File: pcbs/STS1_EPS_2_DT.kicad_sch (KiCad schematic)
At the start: 19 parts, among them Q2 SI7272DP-T1-GE3, Q3 2N7002, U1 4072, U2 LTC6995IDCB-1

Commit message: Fixed some warnings and errors.
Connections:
- net +5V is gone; now on net V_LOGIC: R7.1
- net GND: no longer U1.1
- no-connect marks 0 -> 1
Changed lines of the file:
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@@
 		(color 0 0 0 0)
 	)
+	(no_connect
+		(at 107.95 113.03)
+	)
 	(wire
 		(pts
@@
 	(wire
 		(pts
+			(xy 107.95 113.03) (xy 105.41 113.03)
+		)
+		(stroke
+			(width 0)
+			(type default)
+		)
+	)
+	(wire
+		(pts
 			(xy 128.27 135.89) (xy 128.27 137.16)
 		)
@@
 		)
 	)
-	(hierarchical_label "V_LOGIC"
-		(shape input)
-		(at 120.65 120.65 180)
+	(hierarchical_label "DT_SIGNAL"
+		(shape output)
+		(at 273.05 73.66 0)
 		(fields_autoplaced yes)
 		(effects
@@
 				(size 1.27 1.27)
 			)
-			(justify right)
+			(justify left)
 		)
 	)
-	(hierarchical_label "DT_SIGNAL"
-		(shape output)
-		(at 273.05 73.66 0)
+	(hierarchical_label "V_LOGIC"
+		(shape input)
+		(at 97.79 20.32 0)
 		(fields_autoplaced yes)
 		(effects
@@
 	(hierarchical_label "V_LOGIC"
 		(shape input)
-		(at 97.79 20.32 0)
+		(at 128.27 121.92 180)
 		(fields_autoplaced yes)
 		(effects
@@
 				(size 1.27 1.27)
 			)
-			(justify left)
+			(justify right)
 		)
 	)
@@
 	(symbol
 		(lib_id "power:GND")
-		(at 105.41 113.03 90)
-		(unit 1)
-		(exclude_from_sim no)
-		(in_bom yes)
-		(on_board yes)
-		(dnp no)
-		(fields_autoplaced yes)
-		(property "Reference" "#PWR024"
-			(at 111.76 113.03 0)
-			(effects
-				(font
-					(size 1.27 1.27)
-				)
-				(hide yes)
-			)
-		)
-		(property "Value" "GND"
-			(at 109.22 113.0299 90)
-			(effects
-				(font
-					(size 1.27 1.27)
-				)
-				(justify right)
-			)
-		)
-		(property "Footprint" ""
-			(at 105.41 113.03 0)
-			(effects
-				(font
-					(size 1.27 1.27)
-				)
-				(hide yes)
-			)
-		)
-		(property "Datasheet" ""
-			(at 105.41 113.03 0)
-			(effects
-				(font
-					(size 1.27 1.27)
-				)
-				(hide yes)
-			)
-		)
-		(property "Description" ""
-			(at 105.41 113.03 0)
-			(effects
-				(font
-					(size 1.27 1.27)
-				)
-				(hide yes)
-			)
-		)
-		(pin "1"
-		)
-		(instances
-			(project "STS1_EPS_2"
-				(path "/38c03ff7-ea47-4d00-b37d-ddcaa7d87722/d08cc104-26df-403e-aeed-bb3c2e21e328"
-					(reference "#PWR024")
-					(unit 1)
-				)
-			)
-		)
-	)
-	(symbol
-		(lib_id "power:GND")
 		(at 90.17 111.76 270)
 		(unit 1)
@@
 			)
 		)
-		(property "Description" ""
+		(property "Description" "Power symbol creates a global label with name \"GND\" , ground"
 			(at 90.17 111.76 0)
 			(effects
@@
 			)
 		)
-		(property "Description" ""
+		(property "Description" "Power symbol creates a global label with name \"GND\" , ground"
 			(at 90.17 114.3 0)
 			(effects
@@
 			)
 		)
-		(property "Description" ""
+		(property "Description" "Power symbol creates a global label with name \"GND\" , ground"
 			(at 148.59 97.79 0)
 			(effects
@@
 			)
 		)
-		(property "Description" ""
+		(property "Description" "Power symbol creates a global label with name \"GND\" , ground"
 			(at 146.05 129.54 0)
 			(effects
@@
 			)
 		)
-		(property "Description" ""
+		(property "Description" "Power symbol creates a global label with name \"GND\" , ground"
 			(at 196.85 97.79 0)
 			(effects
@@
 			)
 		)
-		(property "Description" ""
+		(property "Description" "Power symbol creates a global label with name \"GND\" , ground"
 			(at 158.75 85.09 0)
 			(effects
@@
 			)
 		)
-		(property "Description" ""
+		(property "Description" "Power symbol creates a global label with name \"GND\" , ground"
 			(at 90.17 99.06 0)
 			(effects
@@
 			)
 		)
-		(property "Description" ""
+		(property "Description" "Power symbol creates a global label with name \"GND\" , ground"
 			(at 219.71 97.79 0)
 			(effects
@@
 			)
 		)
-		(property "Description" ""
+		(property "Description" "Power symbol creates a global label with name \"GND\" , ground"
 			(at 90.17 109.22 0)
 			(effects
@@
 			)
 		)
-		(property "Description" ""
+		(property "Description" "0.115A Id, 60V Vds, N-Channel MOSFET, SOT-23"
 			(at 234.95 87.63 0)
 			(effects
@@
 			)
 		)
-		(property "Description" ""
+		(property "Description" "Power symbol creates a global label with name \"GND\" , ground"
 			(at 128.27 147.32 0)
 			(effects
@@
 			)
 		)
-		(property "Description" ""
+		(property "Description" "Power symbol creates a global label with name \"GND\" , ground"
 			(at 90.17 116.84 0)
 			(effects
@@
 			)
 		)
-		(property "Description" ""
+		(property "Description" "Power symbol creates a global label with name \"GND\" , ground"
 			(at 175.26 97.79 0)
 			(effects
@@
 			)
 		)
-		(property "Description" ""
+		(property "Description" "Power symbol creates a global label with name \"GND\" , ground"
 			(at 97.79 53.34 0)
 			(effects
@@
 	)
 	(symbol
-		(lib_id "power:+5V")
-		(at 128.27 121.92 0)
-		(unit 1)
-		(exclude_from_sim no)
-		(in_bom yes)
-		(on_board yes)
-		(dnp no)
-		(fields_autoplaced yes)
-		(property "Reference" "#PWR0112"
-			(at 128.27 125.73 0)
-			(effects
-				(font
-					(size 1.27 1.27)
-				)
-				(hide yes)
-			)
-		)
-		(property "Value" "+5V"
-			(at 128.27 116.84 0)
-			(effects
-				(font
-					(size 1.27 1.27)
-				)
-			)
-		)
-		(property "Footprint" ""
-			(at 128.27 121.92 0)
-			(effects
-				(font
-					(size 1.27 1.27)
-				)
-				(hide yes)
-			)
-		)
-		(property "Datasheet" ""
-			(at 128.27 121.92 0)
-			(effects
-				(font
-					(size 1.27 1.27)
-				)
-				(hide yes)
-			)
-		)
-		(property "Description" ""
-			(at 128.27 121.92 0)
-			(effects
-				(font
-					(size 1.27 1.27)
-				)
-				(hide yes)
-			)
-		)
-		(pin "1"
-		)
-		(instances
-			(project "STS1_EPS_2"
-				(path "/38c03ff7-ea47-4d00-b37d-ddcaa7d87722/d08cc104-26df-403e-aeed-bb3c2e21e328"
-					(reference "#PWR0112")
-					(unit 1)
-				)
-			)
-		)
-	)
-	(symbol
 		(lib_id "power:GND")
 		(at 237.49 97.79 0)
@@
 			)
 		)
-		(property "Description" ""
+		(property "Description" "Power symbol creates a global label with name \"GND\" , ground"
 			(at 237.49 97.79 0)
 			(effects

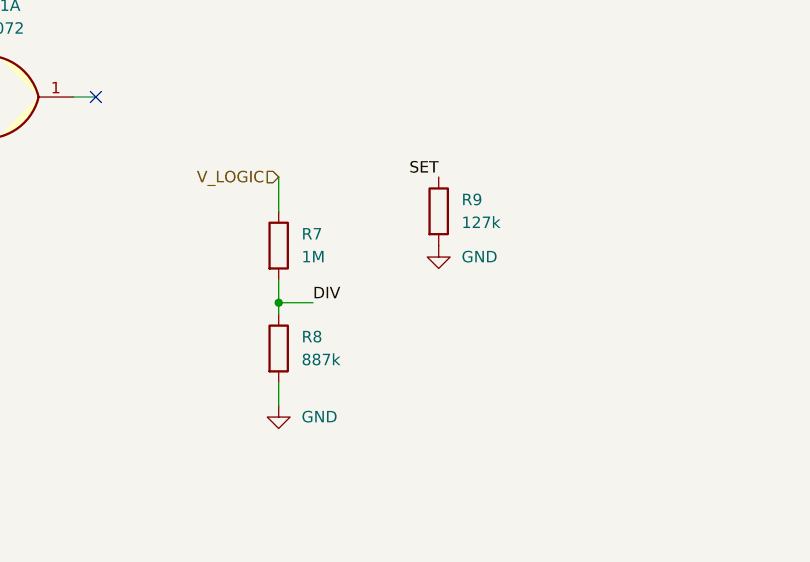
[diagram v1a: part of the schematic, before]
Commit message: Modified some resistor values slightly, so that they fall in common resistor series.
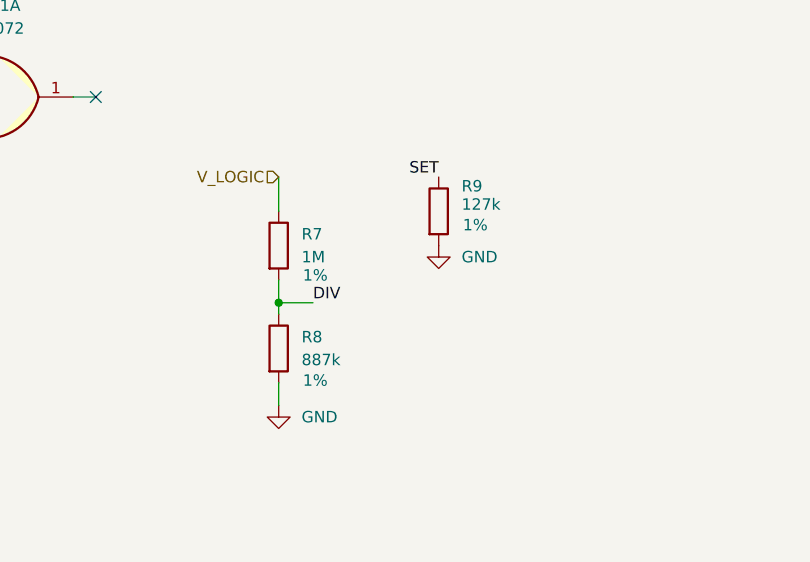
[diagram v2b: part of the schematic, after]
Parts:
- R7, R8, R9: Tolerance (none) -> 1%
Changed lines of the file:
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@@
 		(on_board yes)
 		(dnp no)
-		(fields_autoplaced yes)
 		(property "Reference" "R8"
 			(at 130.81 139.6999 0)
@@
 				)
 				(hide yes)
+			)
+		)
+		(property "Tolerance" "1%"
+			(at 132.334 144.526 0)
+			(effects
+				(font
+					(size 1.27 1.27)
+				)
 			)
 		)
@@
 		(on_board yes)
 		(dnp no)
-		(fields_autoplaced yes)
 		(property "Reference" "R7"
 			(at 130.81 128.2699 0)
@@
 				)
 				(hide yes)
+			)
+		)
+		(property "Tolerance" "1%"
+			(at 132.334 132.842 0)
+			(effects
+				(font
+					(size 1.27 1.27)
+				)
 			)
 		)
@@
 		(on_board yes)
 		(dnp no)
-		(fields_autoplaced yes)
 		(property "Reference" "R9"
-			(at 148.59 124.4599 0)
+			(at 148.59 122.9359 0)
 			(effects
 				(font
@@
 		)
 		(property "Value" "127k"
-			(at 148.59 126.9999 0)
+			(at 148.59 124.968 0)
 			(effects
 				(font
@@
 			)
 		)
+		(property "Tolerance" "1%"
+			(at 150.114 127.254 0)
+			(effects
+				(font
+					(size 1.27 1.27)
+				)
+			)
+		)

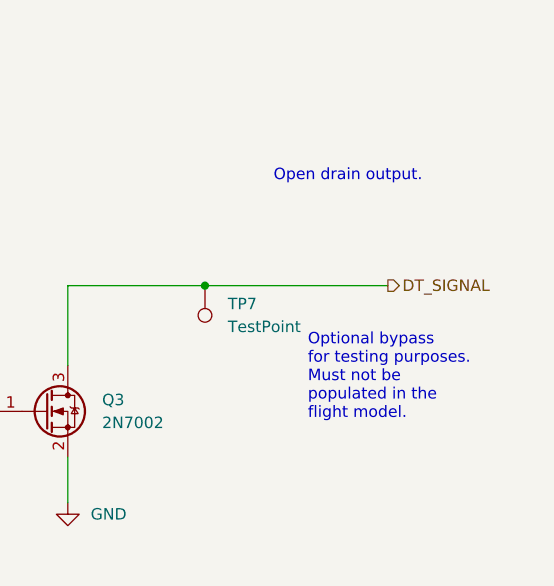
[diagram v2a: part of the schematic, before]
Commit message: Marked optional bypasses as "Do not place".
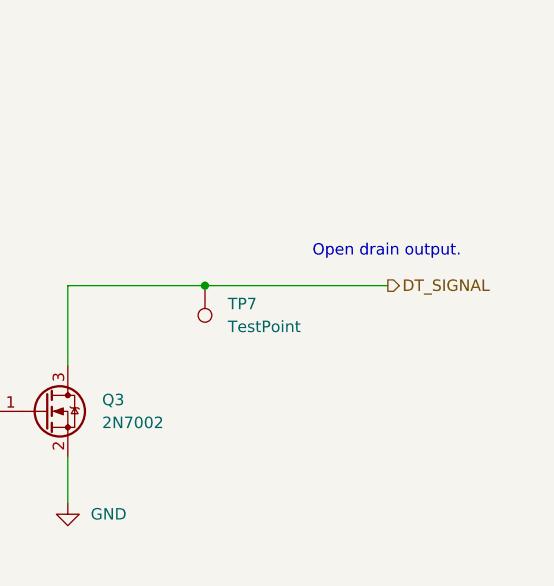
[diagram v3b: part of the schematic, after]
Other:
- note removed: "Optional bypass for testing purposes. Must not be populated in the flight model."
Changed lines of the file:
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@@
 	(text "Open drain output."
 		(exclude_from_sim no)
-		(at 260.35 62.23 0)
+		(at 264.668 70.612 0)
 		(effects
 			(font
@@
 		)
 	)
-	(text "Optional bypass \nfor testing purposes.\nMust not be \npopulated in the \nflight model."
-		(exclude_from_sim no)
-		(at 264.16 83.82 0)
-		(effects
-			(font
-				(size 1.27 1.27)
-			)
-			(justify left)
-		)
-	)

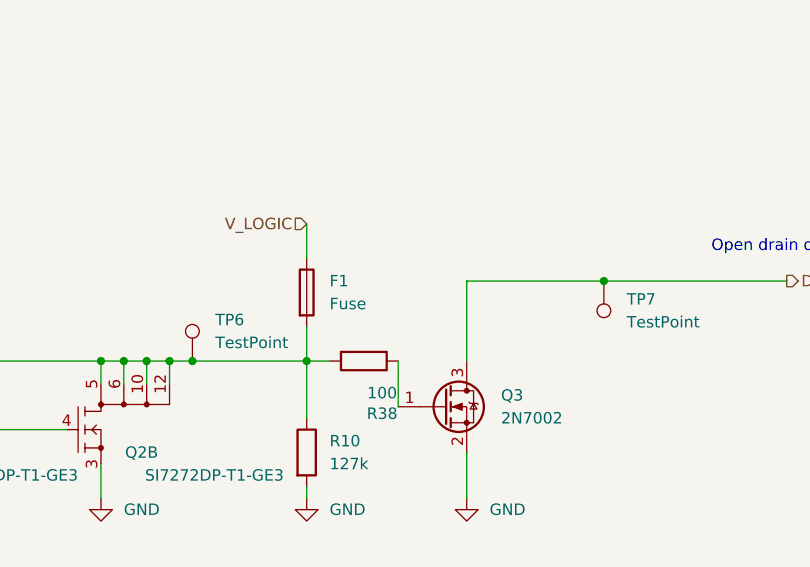
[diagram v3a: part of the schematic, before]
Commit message: Added part number to fuse.
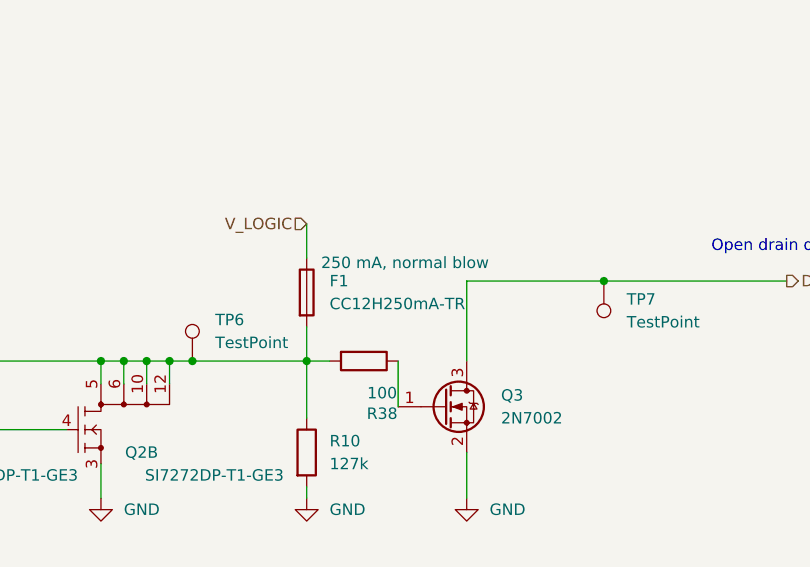
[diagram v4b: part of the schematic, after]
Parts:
- F1: value Fuse -> CC12H250mA-TR
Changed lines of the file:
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@@
 		(on_board yes)
 		(dnp no)
-		(fields_autoplaced yes)
 		(property "Reference" "F1"
 			(at 222.25 73.6599 0)
@@
 			)
 		)
-		(property "Value" "Fuse"
+		(property "Value" "CC12H250mA-TR"
 			(at 222.25 76.1999 0)
 			(effects
@@
 			)
 		)
-		(property "Description" ""
-			(at 219.71 74.93 0)
+		(property "Description" "250 mA, normal blow"
+			(at 230.632 71.628 0)
 			(effects
 				(font
 					(size 1.27 1.27)
 				)
-				(hide yes)
 			)
 		)

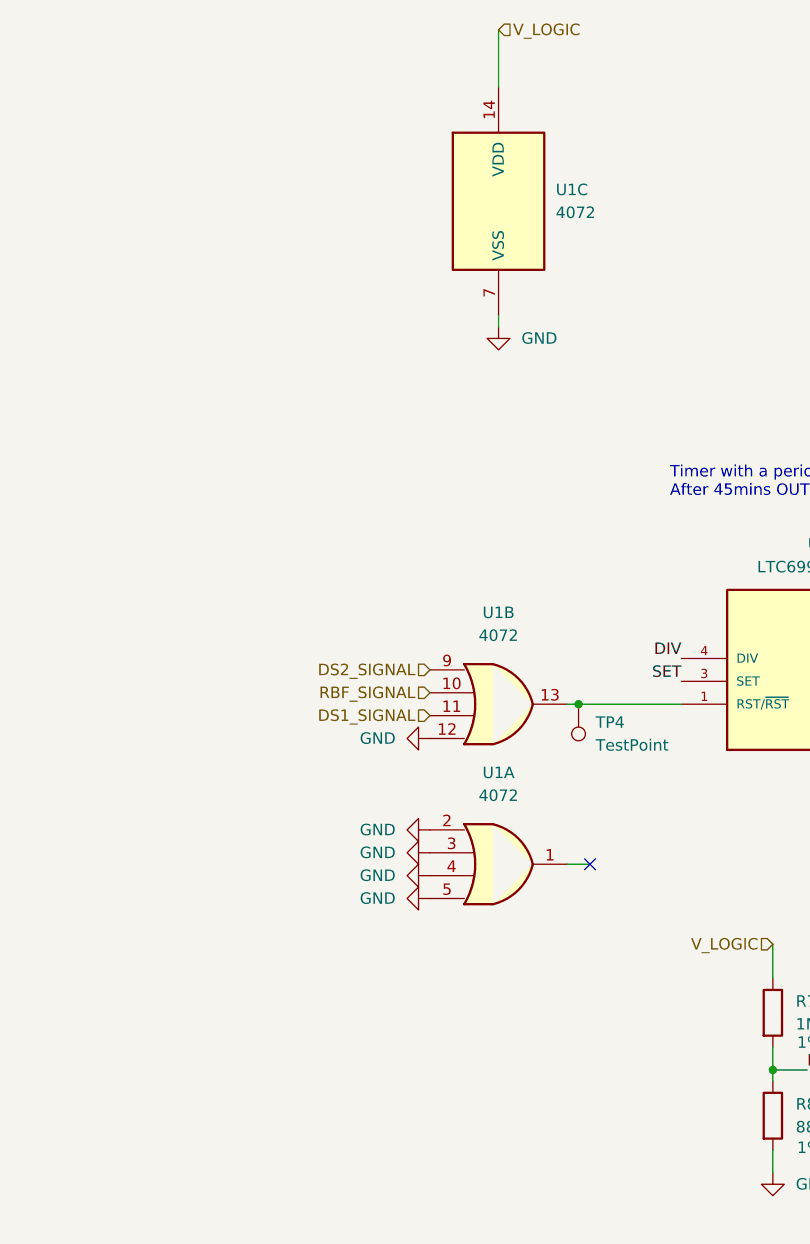
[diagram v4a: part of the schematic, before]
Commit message: Logic gates now use ISO symbols consistently.
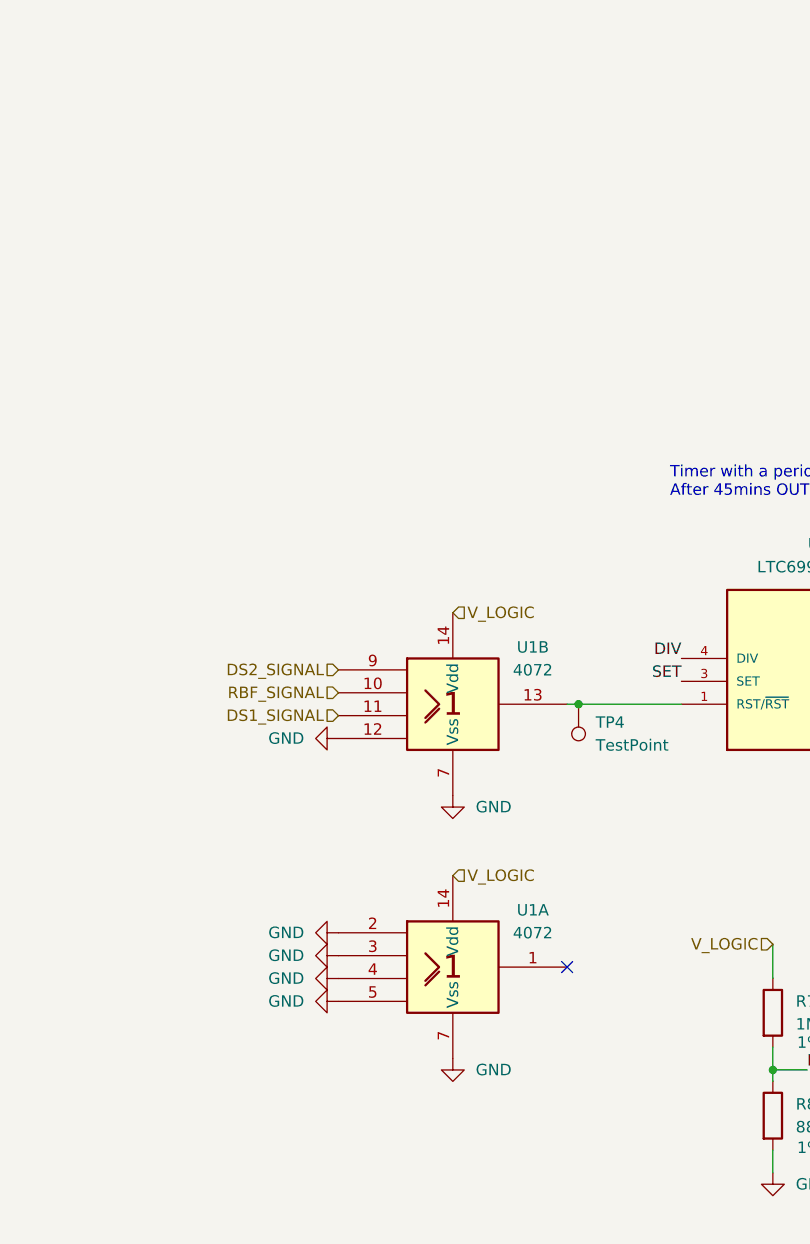
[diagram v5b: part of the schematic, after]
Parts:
- removed unit 1 of U1
- removed unit 3 of U1
- added unit 1 of U1
- U1: symbol 4xxx:4072 -> 4xxx_IEEE:4072
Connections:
- net GND: now also U1.7 (Vss), U1.2, U1.3, U1.4, U1.5, U1.7 (Vss)
- net V_LOGIC: now also U1.14 (Vdd), U1.14 (Vdd)

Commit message: Added more part numbers.
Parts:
- C1: Part Nr. (none) -> C0805T104K1RCLTU
- R1, R2, R5: Part Nr. (none) -> TNPW0805100KFEEA
- R10, R9: Part Nr. (none) -> RN73H2ATTD1273B25
- R11, R38: Part Nr. (none) -> TNPW0805100RFETA
- R7: Part Nr. (none) -> CRT0805-BY-1004ELF
- R8: Part Nr. (none) -> ERA-6AEB8873V
- U1: Part Nr. (none) -> CD4072BM96G4
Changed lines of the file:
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@@
+			)
+		)
+		(property "Part Nr." "ERA-6AEB8873V"
+			(at 128.27 140.97 0)
+			(effects
+				(font
+					(size 1.27 1.27)
+				)
+				(hide yes)
 			)
 		)
@@
 			)
 		)
+		(property "Part Nr." ""
+			(at 151.13 90.17 0)
+			(effects
+				(font
+					(size 1.27 1.27)
+				)
+				(hide yes)
+			)
+		)
 		(pin "1"
 		)
@@
 			)
 		)
+		(property "Part Nr." ""
+			(at 133.35 90.17 0)
+			(effects
+				(font
+					(size 1.27 1.27)
+				)
+				(hide yes)
+			)
+		)
 		(pin "1"
 		)
@@
 			)
 		)
+		(property "Part Nr." "TNPW0805100KFEEA"
+			(at 33.02 59.69 0)
+			(effects
+				(font
+					(size 1.27 1.27)
+				)
+				(hide yes)
+			)
+		)
 		(pin "1"
 		)
@@
 			)
 		)
+		(property "Part Nr." ""
+			(at 252.73 73.66 0)
+			(effects
+				(font
+					(size 1.27 1.27)
+				)
+				(hide yes)
+			)
+		)
 		(pin "1"
 		)
@@
 			)
 		)
+		(property "Part Nr." ""
+			(at 171.45 90.17 0)
+			(effects
+				(font
+					(size 1.27 1.27)
+				)
+				(hide yes)
+			)
+		)
 		(pin "1"
 		)
@@
 					(size 1.27 1.27)
 				)
+			)
+		)
+		(property "Part Nr." "CRT0805-BY-1004ELF"
+			(at 128.27 129.54 0)
+			(effects
+				(font
+					(size 1.27 1.27)
+				)
+				(hide yes)
 			)
 		)
@@
 			)
 		)
+		(property "Part Nr." ""
+			(at 106.68 95.25 0)
+			(effects
+				(font
+					(size 1.27 1.27)
+				)
+				(hide yes)
+			)
+		)
 		(pin "1"
 		)
@@
 					(size 1.27 1.27)
 				)
+			)
+		)
+		(property "Part Nr." "RN73H2ATTD1273B25"
+			(at 146.05 125.73 0)
+			(effects
+				(font
+					(size 1.27 1.27)
+				)
+				(hide yes)
 			)
 		)
@@
 			)
 		)
+		(property "Part Nr." ""
+			(at 193.04 90.17 0)
+			(effects
+				(font
+					(size 1.27 1.27)
+				)
+				(hide yes)
+			)
+		)
 		(pin "1"
 		)
@@
 		)
 		(property "Description" ""
+			(at 226.06 82.55 0)
+			(effects
+				(font
+					(size 1.27 1.27)
+				)
+				(hide yes)
+			)
+		)
+		(property "Part Nr." "TNPW0805100RFETA"
 			(at 226.06 82.55 0)
 			(effects
@@
 			)
 		)
+		(property "Part Nr." ""
+			(at 207.01 82.55 0)
+			(effects
+				(font
+					(size 1.27 1.27)
+				)
+				(hide yes)
+			)
+		)
 		(pin "1"
 		)
@@
 			)
 		)
+		(property "Part Nr." "CD4072BM96G4"
+			(at 92.71 95.25 0)
+			(effects
+				(font
+					(size 1.27 1.27)
+				)
+				(hide yes)
+			)
+		)
 		(pin "1"
 		)
@@
 			)
 		)
+		(property "Part Nr." "TNPW0805100RFETA"
+			(at 165.1 90.17 0)
+			(effects
+				(font
+					(size 1.27 1.27)
+				)
+				(hide yes)
+			)
+		)
 		(pin "1"
 		)
@@
 			)
 		)
+		(property "Part Nr." ""
+			(at 219.71 74.93 0)
+			(effects
+				(font
+					(size 1.27 1.27)
+				)
+				(hide yes)
+			)
+		)
 		(pin "1"
 		)
@@
 			)
 		)
+		(property "Part Nr." "TNPW0805100KFEEA"
+			(at 33.02 77.47 0)
+			(effects
+				(font
+					(size 1.27 1.27)
+				)
+				(hide yes)
+			)
+		)
 		(pin "1"
 		)
@@
 			)
 		)
+		(property "Part Nr." ""
+			(at 234.95 87.63 0)
+			(effects
+				(font
+					(size 1.27 1.27)
+				)
+				(hide yes)
+			)
+		)
 		(pin "1"
 		)
@@
 			)
 		)
+		(property "Part Nr." "TNPW0805100KFEEA"
+			(at 33.02 154.94 0)
+			(effects
+				(font
+					(size 1.27 1.27)
+				)
+				(hide yes)
+			)
+		)
 		(pin "1"
 		)
@@
 			)
 		)
+		(property "Part Nr." "RN73H2ATTD1273B25"
+			(at 219.71 92.71 0)
+			(effects
+				(font
+					(size 1.27 1.27)
+				)
+				(hide yes)
+			)
+		)
 		(pin "1"
 		)
@@
 			)
 		)
+		(property "Part Nr." "CD4072BM96G4"
+			(at 92.71 124.46 0)
+			(effects
+				(font
+					(size 1.27 1.27)
+				)
+				(hide yes)
+			)
+		)
 		(pin "1"
 		)
@@
 			(at 154.94 85.09 0)
 			(effects
+				(font
+					(size 1.27 1.27)
+				)
+				(hide yes)
+			)
+		)
+		(property "Part Nr." "C0805T104K1RCLTU"
+			(at 154.94 85.09 0)
+			(effects
